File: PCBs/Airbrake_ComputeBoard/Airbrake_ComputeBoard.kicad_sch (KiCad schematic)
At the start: 24 parts, among them Q1 PNP, Q2 PNP, Q3 PNP, Q4 PNP

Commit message: created pcb footprint
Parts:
- added BZ1: Buzzer, Buzzer_Beeper:Buzzer_12x9.5RM7.6, symbol Device:Buzzer
- Q1, Q2, Q3, Q4: footprint (none) -> Package_TO_SOT_SMD:SOT-23
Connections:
- net BK: now also Teensy4.1.4 (PWM); no longer Teensy4.1.5 (PWM)
- net EN: now also Teensy4.1.5 (PWM); no longer Teensy4.1.4 (PWM)
- net F/R: now also Teensy4.1.6 (PWM); no longer Teensy4.1.3 (PWM)
- net GND: now also BZ1.2 (-)
- net SV: now also Teensy4.1.3 (PWM); no longer Teensy4.1.6 (PWM)
- net buzzer: now reaches Teensy4.1.44 (PWM)
- net buzzer: now also BZ1.1 (+)
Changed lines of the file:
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@@
 	(wire
 		(pts
-			(xy 78.74 86.36) (xy 82.55 86.36)
-		)
-		(stroke
-			(width 0)
-			(type default)
-		)
-	)
-	(wire
-		(pts
 			(xy 186.69 63.5) (xy 157.48 63.5)
 		)
@@
 	(wire
 		(pts
-			(xy 78.74 91.44) (xy 82.55 91.44)
-		)
-		(stroke
-			(width 0)
-			(type default)
-		)
-	)
-	(wire
-		(pts
 			(xy 105.41 93.98) (xy 109.22 93.98)
 		)
@@
 	(wire
 		(pts
+			(xy 78.74 91.44) (xy 82.55 91.44)
+		)
+		(stroke
+			(width 0)
+			(type default)
+		)
+	)
+	(wire
+		(pts
 			(xy 199.39 57.15) (xy 199.39 55.88)
 		)
@@
 	(wire
 		(pts
+			(xy 78.74 83.82) (xy 82.55 83.82)
+		)
+		(stroke
+			(width 0)
+			(type default)
+		)
+	)
+	(wire
+		(pts
 			(xy 177.8 67.31) (xy 177.8 74.93)
 		)
@@
 	(wire
 		(pts
-			(xy 125.73 55.88) (xy 125.73 58.42)
+			(xy 78.74 88.9) (xy 82.55 88.9)
 		)
 		(stroke
@@
 	(wire
 		(pts
-			(xy 78.74 55.88) (xy 78.74 58.42)
+			(xy 125.73 55.88) (xy 125.73 58.42)
 		)
 		(stroke
@@
 	(wire
 		(pts
-			(xy 205.74 80.01) (xy 207.01 80.01)
+			(xy 78.74 86.36) (xy 82.55 86.36)
 		)
 		(stroke
@@
 	(wire
 		(pts
-			(xy 143.51 125.73) (xy 143.51 130.81)
+			(xy 78.74 55.88) (xy 78.74 58.42)
 		)
 		(stroke
@@
 	(wire
 		(pts
-			(xy 105.41 81.28) (xy 109.22 81.28)
+			(xy 205.74 80.01) (xy 207.01 80.01)
 		)
 		(stroke
@@
 	(wire
 		(pts
-			(xy 78.74 88.9) (xy 82.55 88.9)
+			(xy 143.51 125.73) (xy 143.51 130.81)
 		)
 		(stroke
@@
 	(wire
 		(pts
-			(xy 184.15 57.15) (xy 184.15 55.88)
+			(xy 105.41 81.28) (xy 109.22 81.28)
 		)
 		(stroke
@@
 	(wire
 		(pts
-			(xy 124.46 129.54) (xy 124.46 130.81)
+			(xy 184.15 57.15) (xy 184.15 55.88)
 		)
 		(stroke
@@
 	(wire
 		(pts
-			(xy 214.63 86.36) (xy 214.63 85.09)
+			(xy 124.46 129.54) (xy 124.46 130.81)
 		)
 		(stroke
@@
 	(wire
 		(pts
-			(xy 210.82 115.57) (xy 210.82 116.84)
+			(xy 214.63 86.36) (xy 214.63 85.09)
 		)
 		(stroke
@@
 	(wire
 		(pts
-			(xy 160.02 114.3) (xy 160.02 115.57)
+			(xy 210.82 115.57) (xy 210.82 116.84)
 		)
 		(stroke
@@
 	(wire
 		(pts
-			(xy 78.74 83.82) (xy 82.55 83.82)
+			(xy 160.02 114.3) (xy 160.02 115.57)
 		)
 		(stroke
@@
 	)
 	(label "EN"
-		(at 78.74 86.36 180)
+		(at 78.74 88.9 180)
 		(fields_autoplaced yes)
 		(effects
@@
 	)
 	(label "F{slash}R"
-		(at 78.74 83.82 180)
+		(at 78.74 91.44 180)
+		(fields_autoplaced yes)
+		(effects
+			(font
+				(size 1.27 1.27)
+			)
+			(justify right bottom)
+		)
+	)
+	(label "buzzer"
+		(at 129.54 96.52 180)
 		(fields_autoplaced yes)
 		(effects
@@
 	)
 	(label "BK"
-		(at 78.74 88.9 180)
+		(at 78.74 86.36 180)
 		(fields_autoplaced yes)
 		(effects
@@
 	)
 	(label "SV"
-		(at 78.74 91.44 180)
+		(at 78.74 83.82 180)
 		(fields_autoplaced yes)
 		(effects
@@
 		)
 	)
+	(label "buzzer"
+		(at 105.41 83.82 0)
+		(fields_autoplaced yes)
+		(effects
+			(font
+				(size 1.27 1.27)
+			)
+			(justify left bottom)
+		)
+	)
 	(label "ALM_5v"
 		(at 210.82 102.87 0)
@@
 	)
 	(symbol
+		(lib_id "Device:Buzzer")
+		(at 132.08 99.06 0)
+		(unit 1)
+		(exclude_from_sim no)
+		(in_bom yes)
+		(on_board yes)
+		(dnp no)
+		(fields_autoplaced yes)
+		(property "Reference" "BZ1"
+			(at 135.89 97.7899 0)
+			(effects
+				(font
+					(size 1.27 1.27)
+				)
+				(justify left)
+			)
+		)
+		(property "Value" "Buzzer"
+			(at 135.89 100.3299 0)
+			(effects
+				(font
+					(size 1.27 1.27)
+				)
+				(justify left)
+			)
+		)
+		(property "Footprint" "Buzzer_Beeper:Buzzer_12x9.5RM7.6"
+			(at 131.445 96.52 90)
+			(effects
+				(font
+					(size 1.27 1.27)
+				)
+				(hide yes)
+			)
+		)
+		(property "Datasheet" "~"
+			(at 131.445 96.52 90)
+			(effects
+				(font
+					(size 1.27 1.27)
+				)
+				(hide yes)
+			)
+		)
+		(property "Description" "Buzzer, polarized"
+			(at 132.08 99.06 0)
+			(effects
+				(font
+					(size 1.27 1.27)
+				)
+				(hide yes)
+			)
+		)
+		(pin "1"
+		)
+		(pin "2"
+		)
+		(instances
+			(project "Airbrake_ComputeBoard"
+				(path "/a93fadd6-4c47-4cef-bf58-a00d85999e83"
+					(reference "BZ1")
+					(unit 1)
+				)
+			)
+		)
+	)
+	(symbol
+		(lib_id "power:GND")
+		(at 129.54 101.6 270)
+		(unit 1)
+		(exclude_from_sim no)
+		(in_bom yes)
+		(on_board yes)
+		(dnp no)
+		(property "Reference" "#PWR015"
+			(at 123.19 101.6 0)
+			(effects
+				(font
+					(size 1.27 1.27)
+				)
+				(hide yes)
+			)
+		)
+		(property "Value" "GND"
+			(at 124.46 101.6 90)
+			(effects
+				(font
+					(size 1.27 1.27)
+				)
+			)
+		)
+		(property "Footprint" ""
+			(at 129.54 101.6 0)
+			(effects
+				(font
+					(size 1.27 1.27)
+				)
+				(hide yes)
+			)
+		)
+		(property "Datasheet" ""
+			(at 129.54 101.6 0)
+			(effects
+				(font
+					(size 1.27 1.27)
+				)
+				(hide yes)
+			)
+		)
+		(property "Description" "Power symbol creates a global label with name \"GND\" , ground"
+			(at 129.54 101.6 0)
+			(effects
+				(font
+					(size 1.27 1.27)
+				)
+				(hide yes)
+			)
+		)
+		(pin "1"
+		)
+		(instances
+			(project "Airbrake_ComputeBoard"
+				(path "/a93fadd6-4c47-4cef-bf58-a00d85999e83"
+					(reference "#PWR015")
+					(unit 1)
+				)
+			)
+		)
+	)
+	(symbol
 		(lib_id "Simulation_SPICE:PNP")
 		(at 175.26 80.01 0)
@@
 			)
 		)
-		(property "Footprint" ""
+		(property "Footprint" "Package_TO_SOT_SMD:SOT-23"
 			(at 210.82 80.01 0)
 			(effects
@@
 			)
 		)
-		(property "Footprint" ""
+		(property "Footprint" "Package_TO_SOT_SMD:SOT-23"
 			(at 229.87 80.01 0)
 			(effects
@@
 			)
 		)
-		(property "Footprint" ""
+		(property "Footprint" "Package_TO_SOT_SMD:SOT-23"
 			(at 190.5 80.01 0)
 			(effects
@@
 			)
 		)
-		(property "Footprint" ""
+		(property "Footprint" "Package_TO_SOT_SMD:SOT-23"
 			(at 247.65 80.01 0)
 			(effects

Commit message: created compute board v1.1
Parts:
- removed BlueRaven1: Conn_01x04, Connector_JST:JST_XH_B4B-XH-A_1x04_P2.50mm_Vertical, symbol Connector_Generic:Conn_01x04
- removed MotoDriver1: Conn_01x08, Connector_JST:JST_XH_B8B-XH-A_1x08_P2.50mm_Vertical, symbol Connector_Generic:Conn_01x08
- removed R3, R5, R7: 1.7 kOhm, Resistor_THT:R_Axial_DIN0204_L3.6mm_D1.6mm_P7.62mm_Horizontal, symbol Device:R
- removed R4, R6, R8: 3.3 kOhm, Resistor_THT:R_Axial_DIN0204_L3.6mm_D1.6mm_P7.62mm_Horizontal, symbol Device:R
- added BlueRaven1: Conn_01x05, Connector_JST:JST_XH_B5B-XH-A_1x05_P2.50mm_Vertical, symbol Connector_Generic:Conn_01x05
- added Buck_Converter1: ~, Breakout Boards:Buck_Converter, symbol Breakout Boards:Buck_Converter
- added MotorDriver1: Conn_01x06, Connector_JST:JST_XH_B6B-XH-A_1x06_P2.50mm_Vertical, symbol Connector_Generic:Conn_01x06
- R1: value 1.7 kOhm -> 3.3kΩ; footprint Resistor_THT:R_Axial_DIN0204_L3.6mm_D1.6mm_P7.62mm_Horizontal -> Resistor_SMD:R_0805_2012Metric_Pad1.20x1.40mm_HandSolder
- R2: value 3.3 kOhm -> 3.3kΩ; footprint Resistor_THT:R_Axial_DIN0204_L3.6mm_D1.6mm_P7.62mm_Horizontal -> Resistor_SMD:R_0805_2012Metric_Pad1.20x1.40mm_HandSolder
- Teensy4.1: footprint Breakout Boards:Teensy_4.1 -> Breakout Boards:Teensy_4.1_USB
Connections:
- net ALM_5v is gone; now on net SCL: R1.1
- net A_5v is gone; now on net Encoder_A: MotorEncoder1.2 (Pin_2)
- net B_5v is gone; now on net Encoder_B: MotorEncoder1.4 (Pin_4)
- net +3.3V: now also R1.2, R2.1
- net GND: now also Q1.3 (E), Q2.3 (E), Teensy4.1.51 (GND), Teensy4.1.52 (GND), BlueRaven1.4 (Pin_4), BlueRaven1.5 (Pin_5), Buck_Converter1.2 (GND), MotorDriver1.1 (Pin_1); no longer R2.2
- net SDA: now also R2.2
- net at Q2.1 (C): now also MotorDriver1.3 (Pin_3)
- net at Q1.1 (C): now also MotorDriver1.2 (Pin_2)
- net at Q3.1 (C): now also MotorDriver1.4 (Pin_4)
- net at Q4.1 (C): now also MotorDriver1.5 (Pin_5)
- net at PowerSwitch1.1 (Pin_1): now also Buck_Converter1.1 (VIN); no longer Battery1.1 (Pin_1)
- net 5v_switch renamed +5V
- net +5V: now also Buck_Converter1.3 (VO), MotorDriver1.6 (Pin_6); no longer PowerSwitch1.2 (Pin_2), Q1.3 (E), Q2.3 (E)
- removed net ALM_3.3v: R1.2, R2.1, Teensy4.1.10 (PWM)
- net A_3.3v renamed Encoder_A
- net B_3.3v renamed Encoder_B
- net EN renamed Stop
- net F/R renamed Dir
- net PG_3.3v: no longer names the net of Teensy4.1.7 (PWM)
- new net: Battery1.1 (Pin_1), PowerSwitch1.2 (Pin_2)
- new net D+: BlueRaven1.3 (Pin_3), Teensy4.1.50 (usb_D+)
- new net D-: BlueRaven1.2 (Pin_2), Teensy4.1.49 (usb_D-)
- new net usb_5v: BlueRaven1.1 (Pin_1), Teensy4.1.48 (usb_5v)
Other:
- moved on the sheet: MotorEncoder1, PowerSwitch1, SensorBoard1

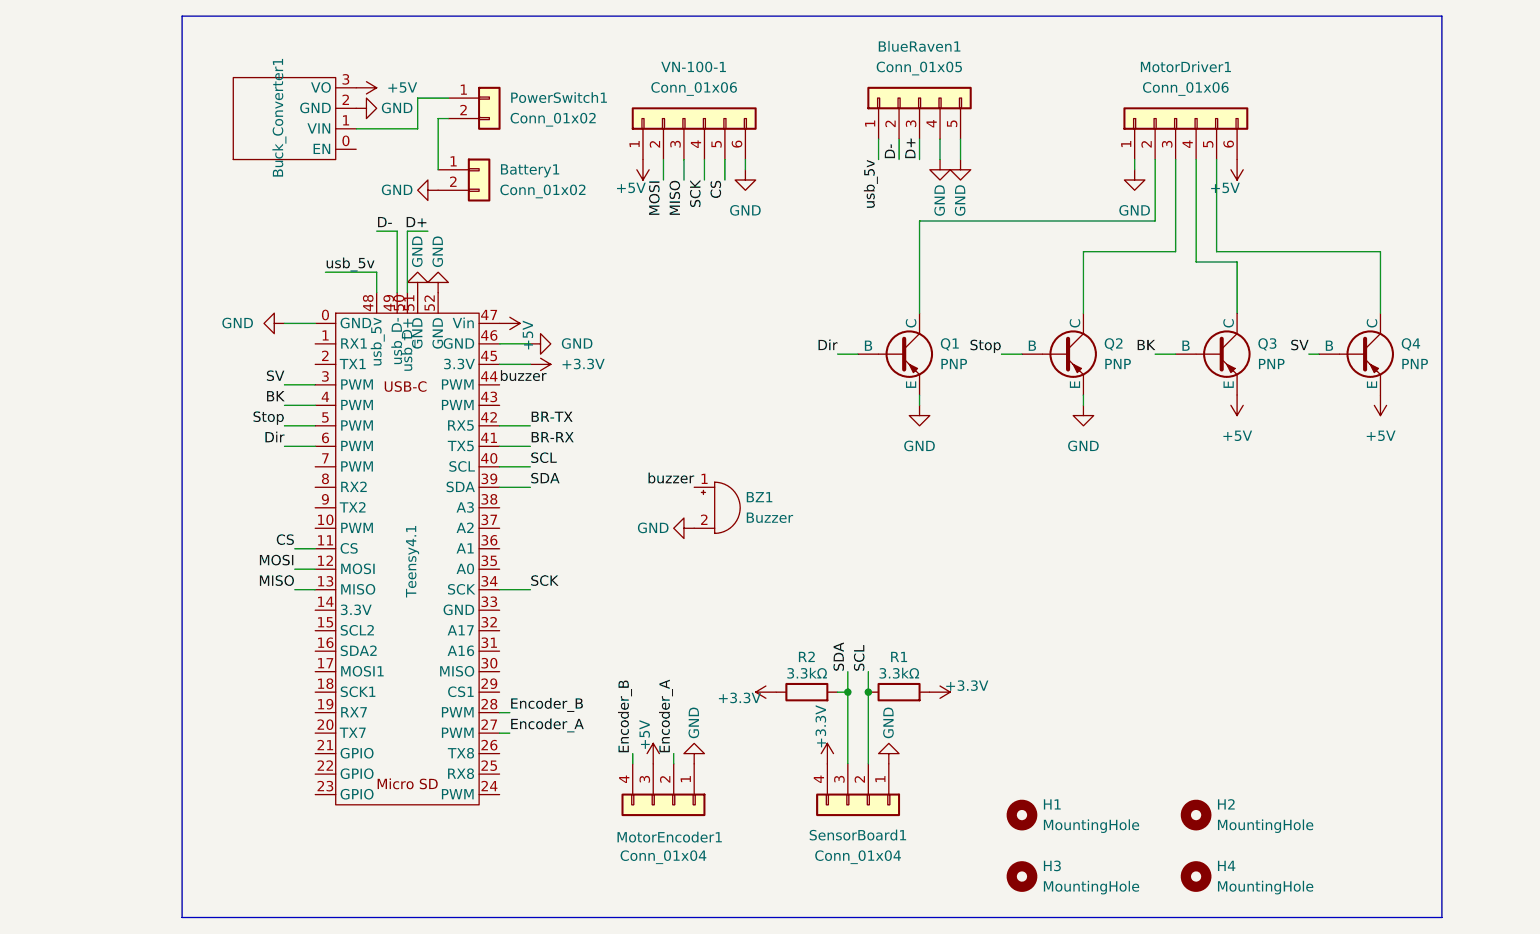
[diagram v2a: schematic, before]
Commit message: Updated level shifter transistors w/ resistors
Added resistors; changed transistors from PNP to NPN; added pull up resistors to output signals.
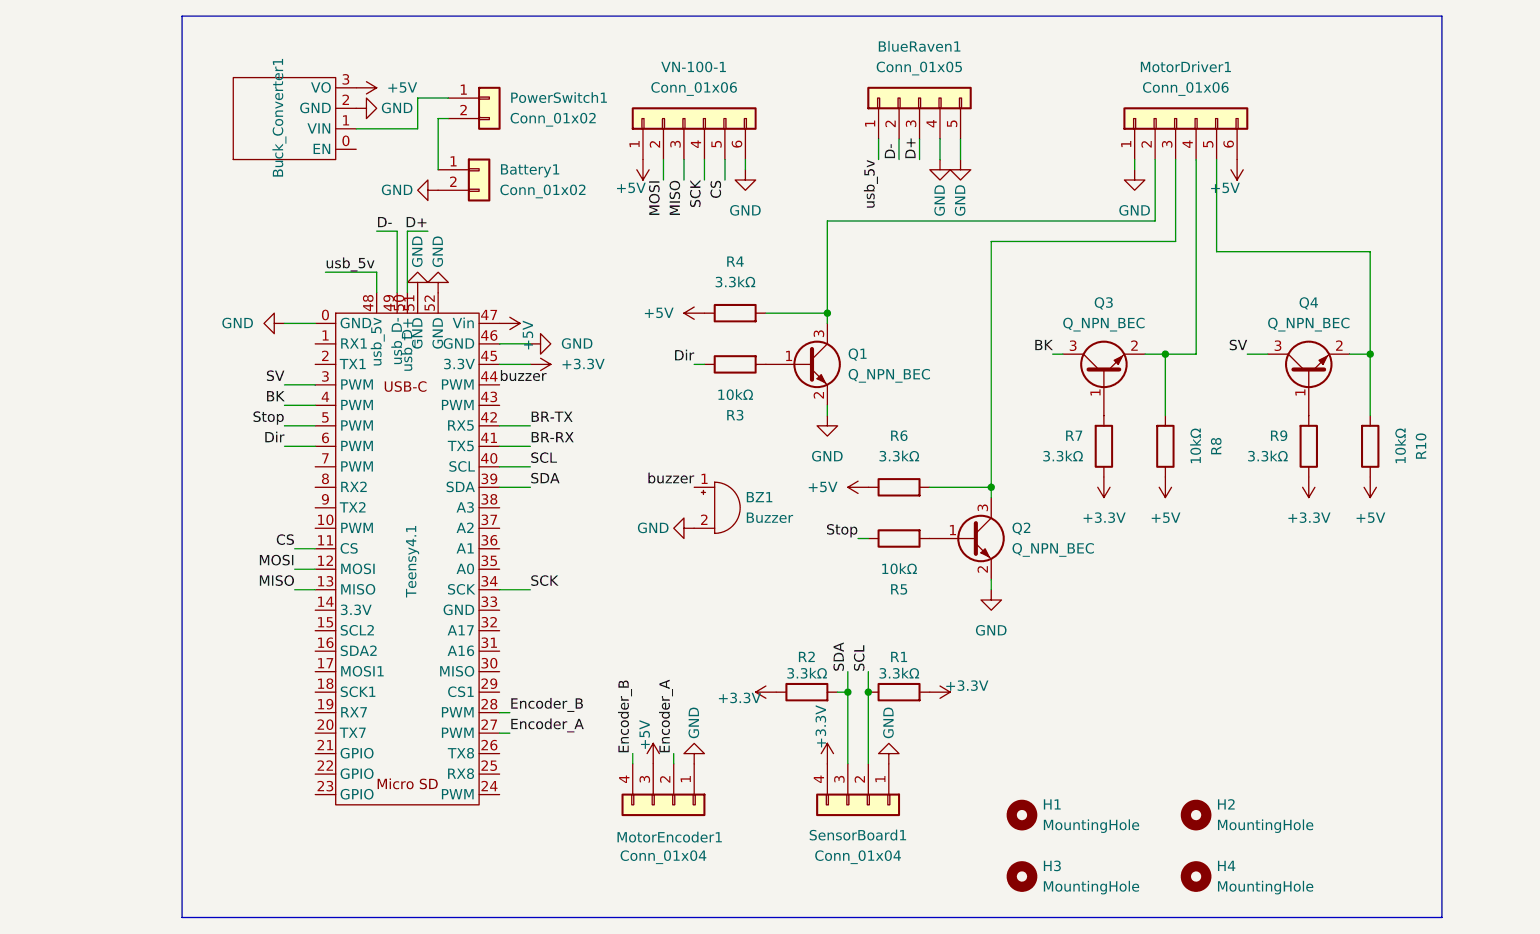
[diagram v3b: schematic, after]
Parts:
- removed Q1, Q2, Q3, Q4: PNP, Package_TO_SOT_SMD:SOT-23, symbol Simulation_SPICE:PNP
- added Q1, Q2, Q3, Q4: Q_NPN_BEC, symbol Device:Q_NPN_BEC
- added R10, R3, R5, R8: 10kΩ, symbol Device:R
- added R4, R6, R7, R9: 3.3kΩ, symbol Device:R
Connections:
- net +3.3V: now also R7.1, R9.1
- net +5V: now also R10.1, R4.1, R6.1, R8.1
- net BK: now also Q3.3 (C)
- net Dir: now also R3.1
- net GND: now also Q1.2 (E), Q2.2 (E)
- net SV: now also Q4.3 (C)
- net Stop: now also R5.1
- net at MotorDriver1.3 (Pin_3): now also Q2.3 (C), R6.2
- net at MotorDriver1.4 (Pin_4): now also Q3.2 (E), R8.2
- net at MotorDriver1.2 (Pin_2): now also Q1.3 (C), R4.2
- net at MotorDriver1.5 (Pin_5): now also Q4.2 (E), R10.2
- new net: Q3.1 (B), R7.2
- new net: Q4.1 (B), R9.2
- new net: Q2.1 (B), R5.2
- new net: Q1.1 (B), R3.2

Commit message: Updated PCB to add resistors to level shifters.
Updated PCB; Added resistors
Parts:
- Q1, Q2, Q3, Q4: footprint (none) -> Package_TO_SOT_SMD:SOT-23
- R10, R3, R4, R5, R6, R7, R8, R9: footprint (none) -> Resistor_SMD:R_0805_2012Metric_Pad1.20x1.40mm_HandSolder
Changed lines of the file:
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@@
 			)
 		)
-		(property "Footprint" ""
+		(property "Footprint" "Package_TO_SOT_SMD:SOT-23"
 			(at 177.8 77.47 0)
 			(effects
@@
 			)
 		)
-		(property "Footprint" ""
+		(property "Footprint" "Package_TO_SOT_SMD:SOT-23"
 			(at 203.2 77.47 0)
 			(effects
@@
 			)
 		)
-		(property "Footprint" ""
+		(property "Footprint" "Resistor_SMD:R_0805_2012Metric_Pad1.20x1.40mm_HandSolder"
 			(at 134.62 76.708 90)
 			(effects
@@
 			)
 		)
-		(property "Footprint" ""
+		(property "Footprint" "Resistor_SMD:R_0805_2012Metric_Pad1.20x1.40mm_HandSolder"
 			(at 154.94 101.092 90)
 			(effects
@@
 			)
 		)
-		(property "Footprint" ""
+		(property "Footprint" "Resistor_SMD:R_0805_2012Metric_Pad1.20x1.40mm_HandSolder"
 			(at 203.962 91.44 90)
 			(effects
@@
 			)
 		)
-		(property "Footprint" ""
+		(property "Footprint" "Package_TO_SOT_SMD:SOT-23"
 			(at 148.59 78.74 0)
 			(effects
@@
 			)
 		)
-		(property "Footprint" ""
+		(property "Footprint" "Resistor_SMD:R_0805_2012Metric_Pad1.20x1.40mm_HandSolder"
 			(at 134.62 79.502 90)
 			(effects
@@
 			)
 		)
-		(property "Footprint" ""
+		(property "Footprint" "Resistor_SMD:R_0805_2012Metric_Pad1.20x1.40mm_HandSolder"
 			(at 186.182 91.44 90)
 			(effects
@@
 			)
 		)
-		(property "Footprint" ""
+		(property "Footprint" "Resistor_SMD:R_0805_2012Metric_Pad1.20x1.40mm_HandSolder"
 			(at 154.94 98.298 90)
 			(effects
@@
 			)
 		)
-		(property "Footprint" ""
+		(property "Footprint" "Resistor_SMD:R_0805_2012Metric_Pad1.20x1.40mm_HandSolder"
 			(at 178.562 91.44 90)
 			(effects
@@
 			)
 		)
-		(property "Footprint" ""
+		(property "Footprint" "Resistor_SMD:R_0805_2012Metric_Pad1.20x1.40mm_HandSolder"
 			(at 211.582 91.44 90)
 			(effects
@@
 			)
 		)
-		(property "Footprint" ""
+		(property "Footprint" "Package_TO_SOT_SMD:SOT-23"
 			(at 168.91 100.33 0)
 			(effects
